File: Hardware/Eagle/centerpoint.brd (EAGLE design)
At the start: 100 x 52.1 mm, 5 parts, among them M1 ARDUINO-NANO-3.0

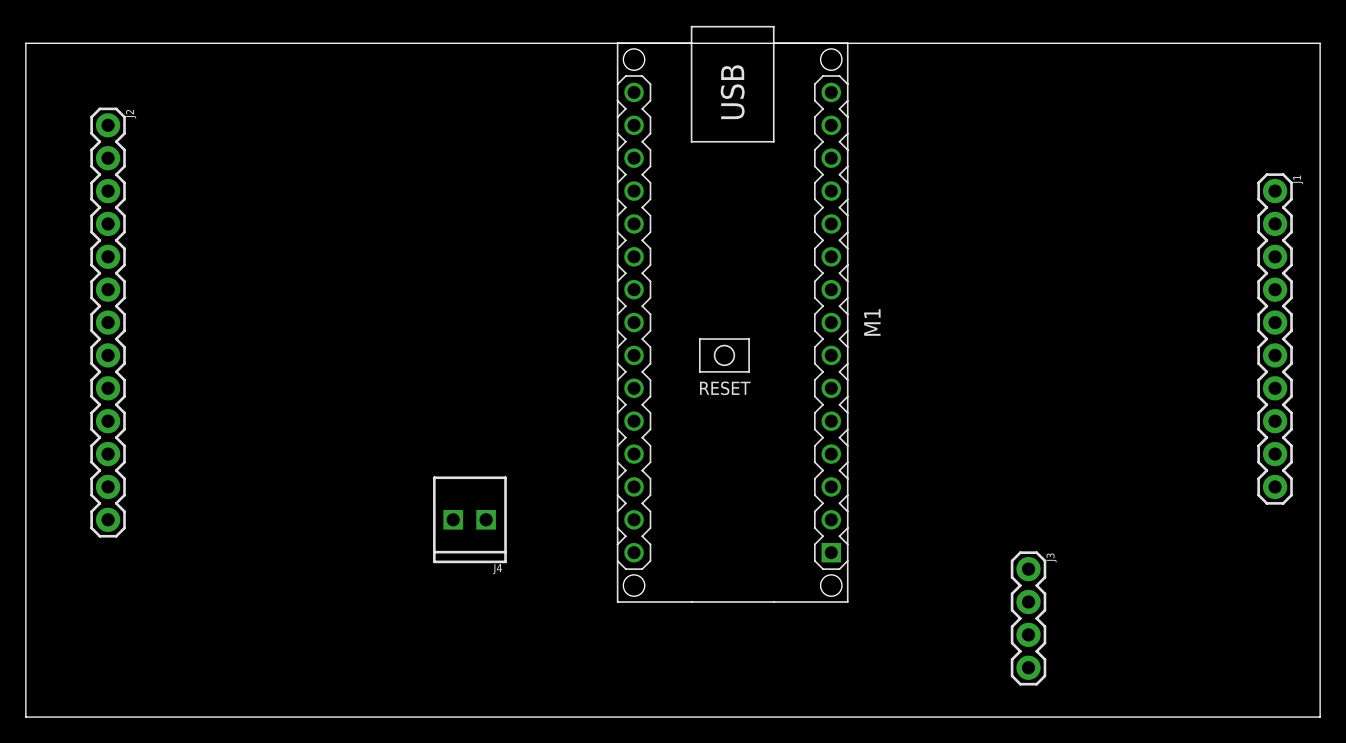
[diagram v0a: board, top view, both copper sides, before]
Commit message: updated adapter board PCB layout
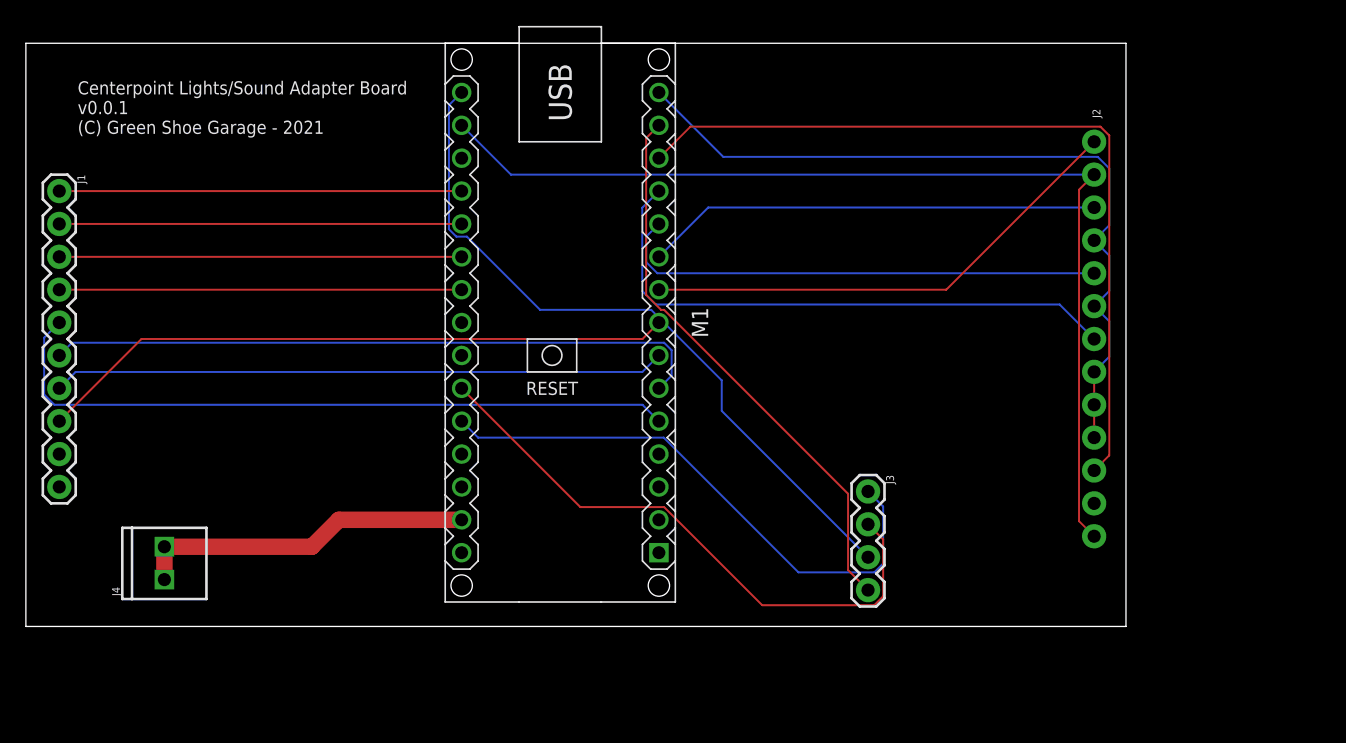
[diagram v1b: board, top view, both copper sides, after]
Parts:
- moved J1 93.9 mm to (2.58, 68.6)
- moved J2 76.2 mm to (82.5, 72.4), flipped to the bottom
- moved J4 25.3 mm to (10.7, 38.6), turned to 90 degrees
- moved J3 13.8 mm to (65.1, 45.4)
- moved M1 13.3 mm to (41.3, 58.4)
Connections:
- net N$17: now also J3.1, M1.J2.5; no longer J3.3, M1.J2.6
- net N$18: now also J3.2, M1.J2.6; no longer J3.1, M1.J2.7
- net N$19: now also J3.3, M1.J2.15; no longer J3.2, M1.J2.8
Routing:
- net N$12: track 0.00 -> 79.4 mm
- net N$9: track 0.00 -> 62.5 mm
- net N$11: track 0.00 -> 60.5 mm
- net N$19: track 0.00 -> 55.2 mm
- net N$1: track 0.00 -> 54.4 mm
- net N$2: track 0.00 -> 51.3 mm
- net N$4: track 0.00 -> 49.5 mm
- net N$3: track 0.00 -> 47.4 mm
- net N$18: track 0.00 -> 45.8 mm
- net N$8: track 0.00 -> 44.7 mm
- net N$17: track 0.00 -> 43.7 mm
- net N$10: track 0.00 -> 43.6 mm
- net N$5: track 0.00 -> 38.4 mm
- net N$7: track 0.00 -> 38.3 mm
- net N$6: track 0.00 -> 35.2 mm
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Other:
- board size 100 x 52.1 mm -> 85 x 45.1 mm
- board text added: "Centerpoint Lights/Sound Adapter Board v0.0.1 (C) Green Shoe Garage - 2021"

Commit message: corrected placement of GND screw terminal and switch interface header
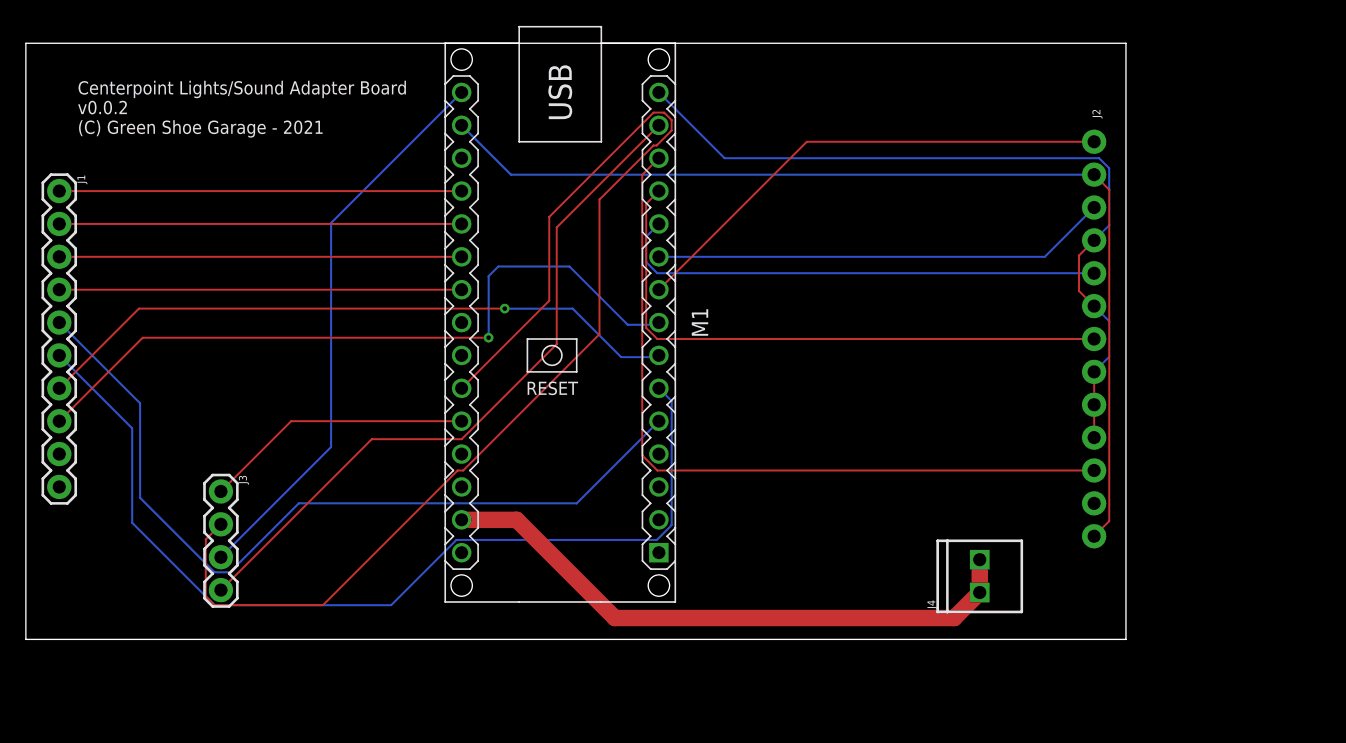
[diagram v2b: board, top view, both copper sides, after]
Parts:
- moved J4 63.0 mm to (73.7, 37.6)
- moved J3 50.0 mm to (15.1, 45.4)
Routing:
- net N$18: track 45.8 -> 93.5 mm
- net N$17: track 43.7 -> 20.8 mm
- net N$2: track 51.3 -> 73.1 mm
- net N$20: track 26.4 -> 46.5 mm
- net N$19: track 55.2 -> 43.6 mm
- net N$10: track 43.6 -> 54.0 mm
- net N$1: track 54.4 -> 63.4 mm
- net N$4: track 49.5 -> 56.2 mm, vias 0 -> 1
- net N$9: track 62.5 -> 58.9 mm
- net N$3: track 47.4 -> 50.5 mm, vias 0 -> 1
- net N$8: track 44.7 -> 45.9 mm
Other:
- board size 85 x 45.1 mm -> 85 x 46.1 mm
- board text added: "Centerpoint Lights/Sound Adapter Board v0.0.2 (C) Green Shoe Garage - 2021"
- board text removed: "Centerpoint Lights/Sound Adapter Board v0.0.1 (C) Green Shoe Garage - 2021"

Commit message: added to silkscreen, change from 2.54 to 5mm screw terminal
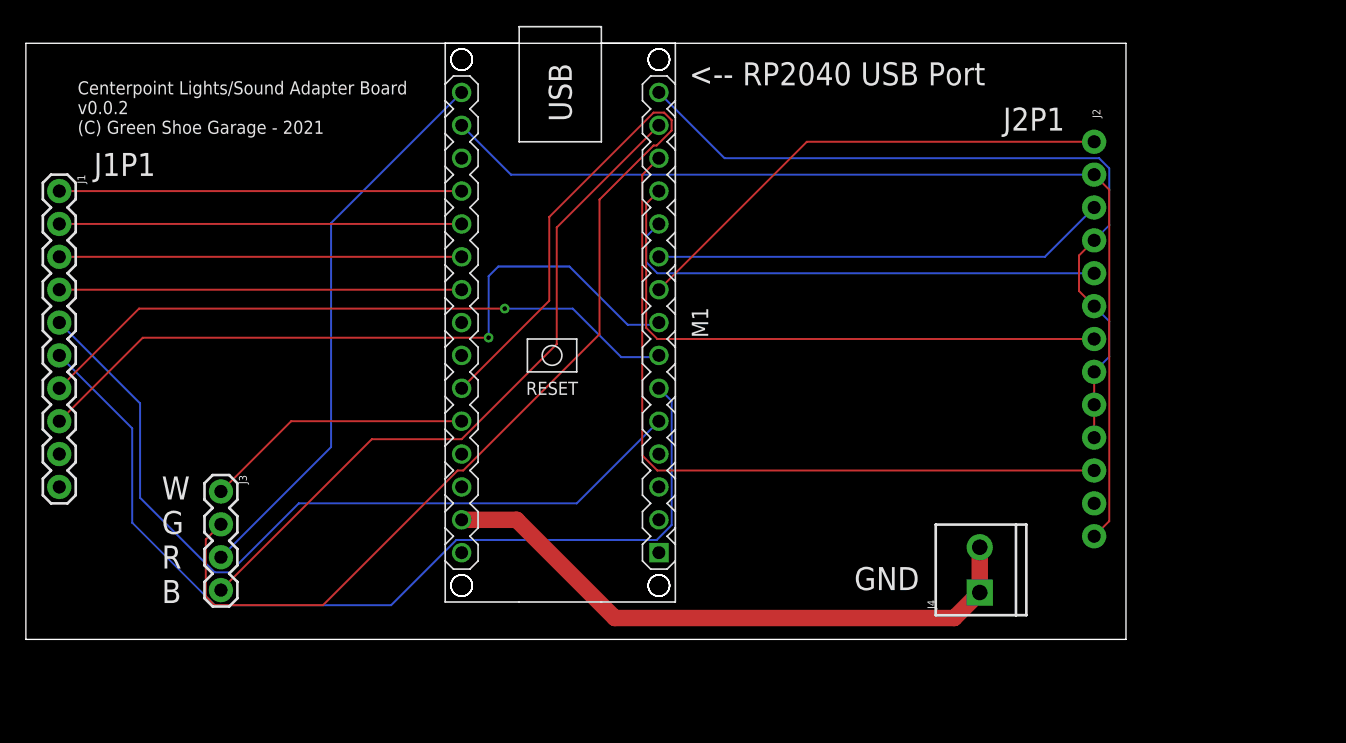
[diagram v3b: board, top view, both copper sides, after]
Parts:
- J4: device SparkFun-Connectors:1X02_2.54_SCREWTERM -> SparkFun-Connectors:SCREWTERMINAL-3.5MM-2
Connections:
- net N$20: now also J4.1, J4.2; no longer J4.P1, J4.P2
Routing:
- net N$20: track 46.5 -> 47.5 mm
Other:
- outline, holes or cut-outs redrawn
- board text added: "<-- RP2040 USB Port"
- board text added: "GND"
- board text added: "J1P1"
- board text added: "J2P1"
- board text added: "W G R B"

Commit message: reworked board layout
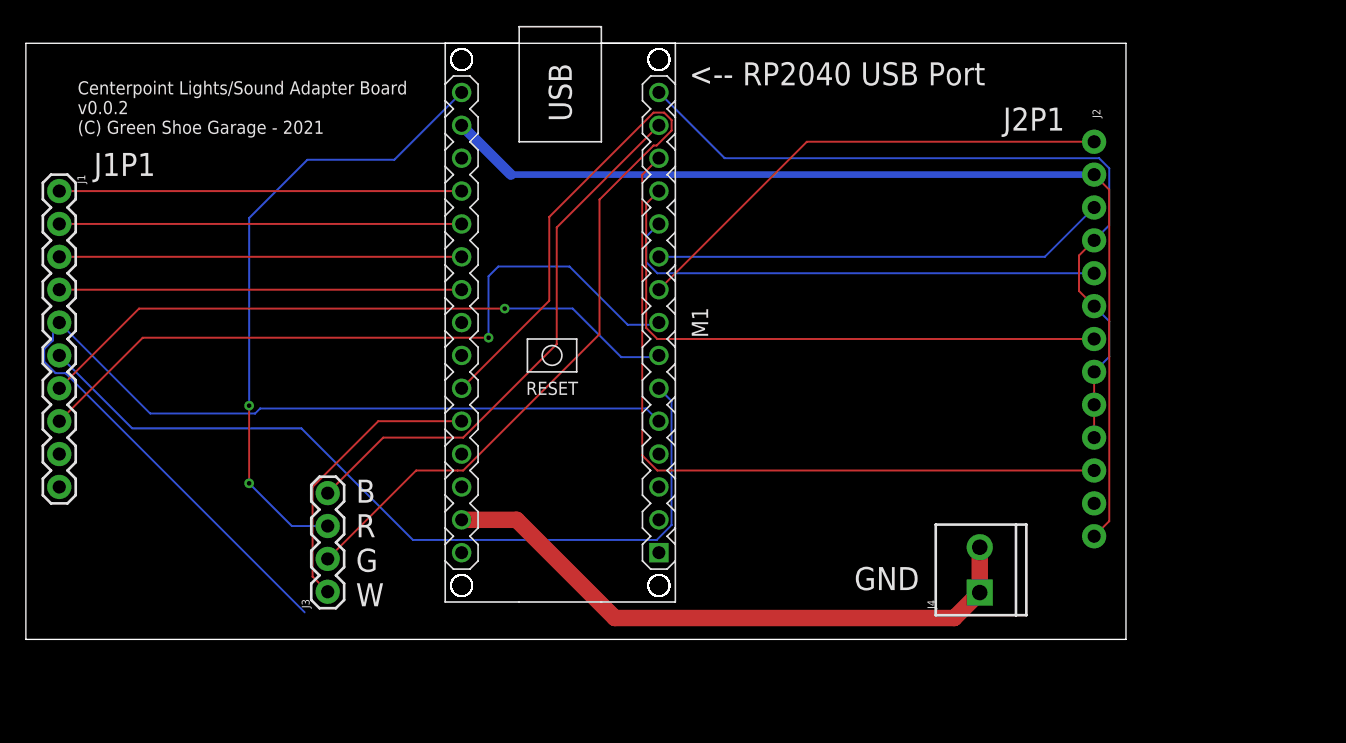
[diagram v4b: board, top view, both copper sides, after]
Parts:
- moved J3 11.3 mm to (23.3, 37.6), turned to 90 degrees
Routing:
- net N$1: track 63.4 -> 81.5 mm
- net N$18: track 93.5 -> 76.3 mm
- net N$10: track 54.0 -> 42.6 mm
- net N$2: track 73.1 -> 64.7 mm
- net N$19: track 43.6 -> 48.4 mm, vias 0 -> 2
- net N$17: track 20.8 -> 22.2 mm
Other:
- outline, holes or cut-outs redrawn
- board text added: "B R G W"
- board text removed: "W G R B"

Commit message: added power switch and screw terminal for battery (VIN)
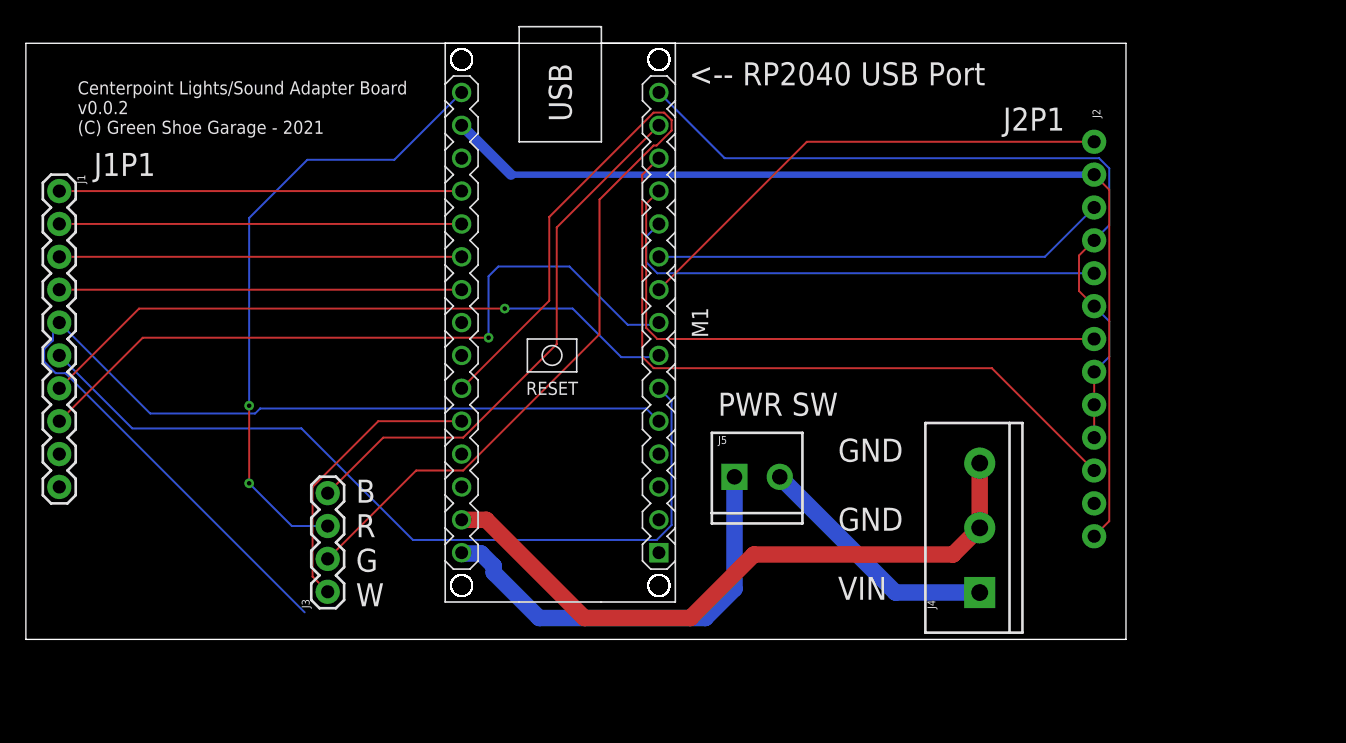
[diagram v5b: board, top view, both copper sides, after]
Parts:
- added J5: (no value), SparkFun-Connectors:SCREWTERMINAL-3.5MM-2
- J4: device SparkFun-Connectors:SCREWTERMINAL-3.5MM-2 -> SparkFun-Connectors:SCREWTERMINAL-5MM-3
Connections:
- removed net VIN: M1.J2.1
- new net N$21: J5.1, M1.J2.1
- new net N$22: J4.1, J5.2
- net N$20: now also J4.3; no longer J4.1
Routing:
- net N$21: track 0.00 -> 33.1 mm
- net N$22: track 0.00 -> 19.2 mm
- net N$9: track 58.9 -> 54.4 mm
- net N$20: track 47.5 -> 51.1 mm
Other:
- outline, holes or cut-outs redrawn
- board text added: "GND GND VIN"
- board text added: "PWR SW"
- board text removed: "GND"
